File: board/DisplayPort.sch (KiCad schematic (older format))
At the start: 15 parts, among them J8 DISPLAY_PORT, J9 DISPLAY_PORT

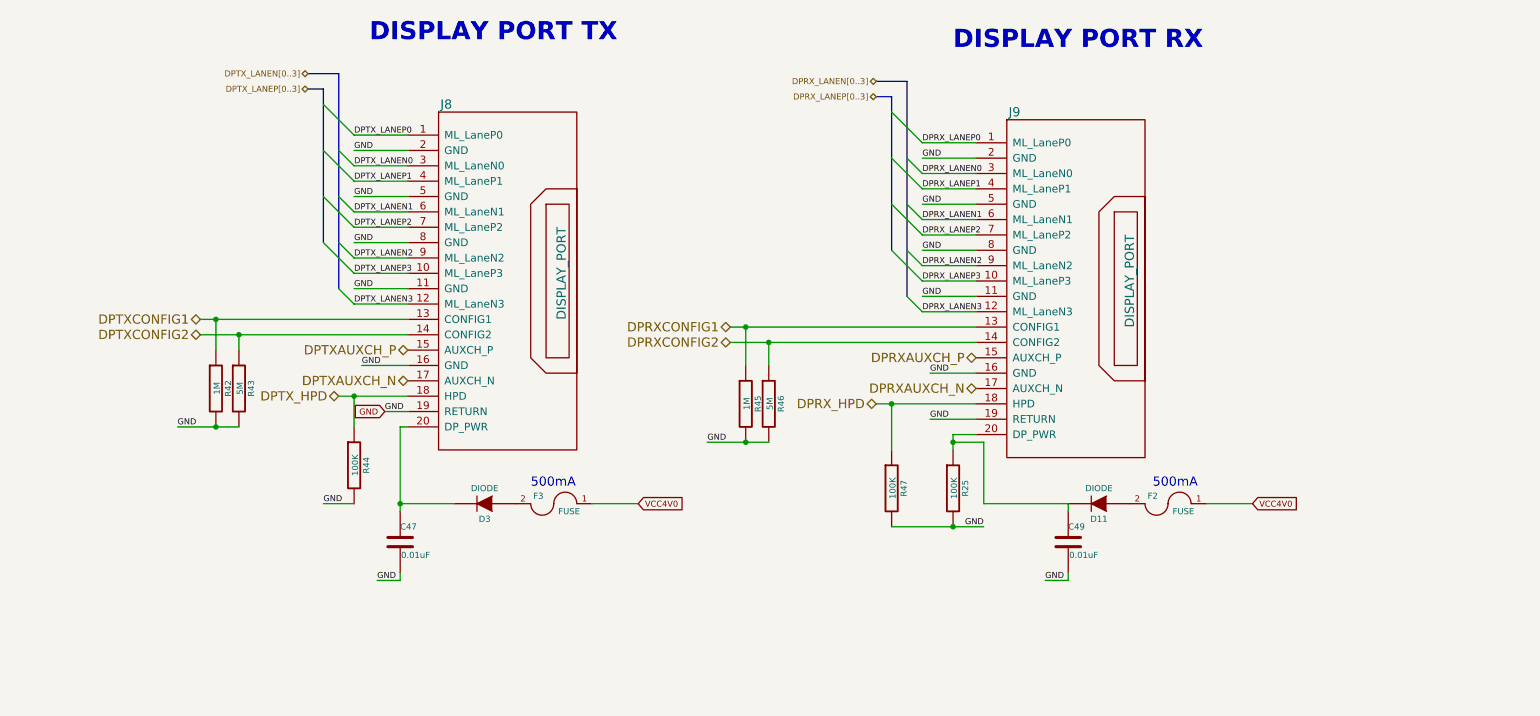
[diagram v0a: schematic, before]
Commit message: Issue #1950 - Adding DisplayPort DC blocking capacitors to schematic.
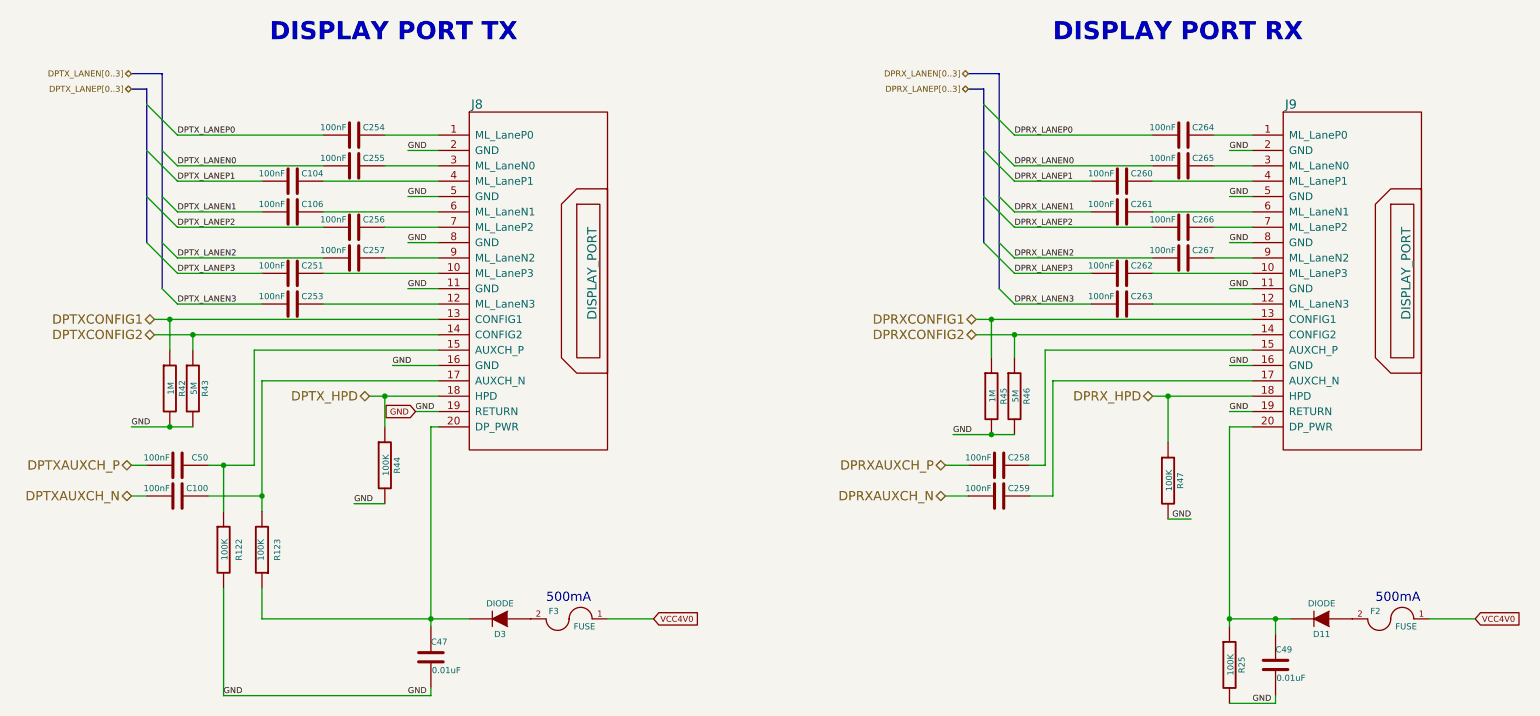
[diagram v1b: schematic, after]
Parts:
- added C100, C104, C106, C251, C253, C254, C255, C256, C257, C258, C259, C260, C261, C262, C263, C264, C265, C266, C267, C50: 100nF, 0402, symbol C
- added R122, R123: 100K, ~, symbol R
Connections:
- net DPRXAUXCH_N: now also C259.1; no longer J9.17 (AUXCH_N)
- net DPRXAUXCH_P: now also C258.1; no longer J9.15 (AUXCH_P)
- net DPRX_LANEN0: now also C265.1; no longer J9.3 (ML_LaneN0)
- net DPRX_LANEN1: now also C261.1; no longer J9.6 (ML_LaneN1)
- net DPRX_LANEN2: now also C267.1; no longer J9.9 (ML_LaneN2)
- net DPRX_LANEN3: now also C263.1; no longer J9.12 (ML_LaneN3)
- net DPRX_LANEP0: now also C264.1; no longer J9.1 (ML_LaneP0)
- net DPRX_LANEP1: now also C260.1; no longer J9.4 (ML_LaneP1)
- net DPRX_LANEP2: now also C266.1; no longer J9.7 (ML_LaneP2)
- net DPRX_LANEP3: now also C262.1; no longer J9.10 (ML_LaneP3)
- net DPTXAUXCH_N: now also C100.1; no longer J8.17 (AUXCH_N)
- net DPTXAUXCH_P: now also C50.1; no longer J8.15 (AUXCH_P)
- net DPTX_LANEN0: now also C255.1; no longer J8.3 (ML_LaneN0)
- net DPTX_LANEN1: now also C106.1; no longer J8.6 (ML_LaneN1)
- net DPTX_LANEN2: now also C257.1; no longer J8.9 (ML_LaneN2)
- net DPTX_LANEN3: now also C253.1; no longer J8.12 (ML_LaneN3)
- net DPTX_LANEP0: now also C254.1; no longer J8.1 (ML_LaneP0)
- net DPTX_LANEP1: now also C104.1; no longer J8.4 (ML_LaneP1)
- net DPTX_LANEP2: now also C256.1; no longer J8.7 (ML_LaneP2)
- net DPTX_LANEP3: now also C251.1; no longer J8.10 (ML_LaneP3)
- net GND: now also R122.2
- net at C47.1, D3.2 (K), J8.20 (DP_PWR): now also R123.1
- new net: C254.2, J8.1 (ML_LaneP0)
- new net: C251.2, J8.10 (ML_LaneP3)
- new net: C253.2, J8.12 (ML_LaneN3)
- new net: C50.2, J8.15 (AUXCH_P), R122.1
- new net: C100.2, J8.17 (AUXCH_N), R123.2
- new net: C255.2, J8.3 (ML_LaneN0)
- new net: C104.2, J8.4 (ML_LaneP1)
- new net: C106.2, J8.6 (ML_LaneN1)
- new net: C256.2, J8.7 (ML_LaneP2)
- new net: C257.2, J8.9 (ML_LaneN2)
- new net: C264.2, J9.1 (ML_LaneP0)
- new net: C262.2, J9.10 (ML_LaneP3)
- new net: C263.2, J9.12 (ML_LaneN3)
- new net: C258.2, J9.15 (AUXCH_P)
- new net: C259.2, J9.17 (AUXCH_N)
- new net: C265.2, J9.3 (ML_LaneN0)
- new net: C260.2, J9.4 (ML_LaneP1)
- new net: C261.2, J9.6 (ML_LaneN1)
- new net: C266.2, J9.7 (ML_LaneP2)
- new net: C267.2, J9.9 (ML_LaneN2)
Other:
- moved on the sheet: C47, C49, D11, D3, F2, F3, J8, J9, R25, R42, R43, R44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

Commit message: Importing footprint names into schematic.
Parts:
- C47, C49, F2, F3, R25, R42, R43, R44, R45, R46, R47: footprint ~ -> SM0603
- D11, D3: footprint ~ -> DO-214AC(SMA)
- J8, J9: footprint ~ -> Display_Port
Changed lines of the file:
@@
 Sheet 6 12
 Title "HDMI2USB"
-Date "5 jul 2015"
+Date "23 jul 2015"
 Rev "Rev2"
 Comp ""
@@
 F 0 "J8" H 3800 4050 60  0000 C CNN
 F 1 "DISPLAY_PORT" V 4550 2950 60  0000 C CNN
-F 2 "~" H 4350 2950 60  0000 C CNN
+F 2 "Display_Port" H 4350 2950 60  0001 C CNN
 F 3 "~" H 4350 2950 60  0000 C CNN
 F 4 "Yes" H 4400 2950 60  0001 C CNN "Populate"
@@
 F 0 "J9" H 9100 4050 60  0000 C CNN
 F 1 "DISPLAY_PORT" V 9850 2950 60  0000 C CNN
-F 2 "~" H 9650 2950 60  0000 C CNN
+F 2 "Display_Port" H 9650 2950 60  0001 C CNN
 F 3 "~" H 9650 2950 60  0000 C CNN
 F 4 "Yes" H 9650 2950 60  0001 C CNN "Populate"
@@
 F 0 "R25" V 8780 5500 40  0000 C CNN
 F 1 "100K" V 8707 5501 40  0000 C CNN
-F 2 "~" V 8630 5500 30  0000 C CNN
+F 2 "SM0603" V 8630 5500 30  0001 C CNN
 F 3 "~" H 8700 5500 30  0000 C CNN
 F 4 "Yes" H 8700 5500 30  0001 C CNN "Populate"
@@
 F 0 "F3" H 4500 5250 40  0000 C CNN
 F 1 "FUSE" H 4300 5150 40  0000 C CNN
-F 2 "~" H 4400 5200 60  0000 C CNN
+F 2 "SM0603" H 4400 5200 60  0001 C CNN
 F 3 "~" H 4400 5200 60  0000 C CNN
 F 4 "Yes" H 4400 5200 60  0001 C CNN "Populate"
@@
 F 0 "R42" V 1880 3700 40  0000 C CNN
 F 1 "1M" V 1807 3701 40  0000 C CNN
-F 2 "~" V 1730 3700 30  0000 C CNN
+F 2 "SM0603" V 1730 3700 30  0001 C CNN
 F 3 "~" H 1800 3700 30  0000 C CNN
 F 4 "Yes" H 1800 3700 30  0001 C CNN "Populate"
@@
 F 0 "R43" V 2030 3700 40  0000 C CNN
 F 1 "5M" V 1957 3701 40  0000 C CNN
-F 2 "~" V 1880 3700 30  0000 C CNN
+F 2 "SM0603" V 1880 3700 30  0001 C CNN
 F 3 "~" H 1950 3700 30  0000 C CNN
 F 4 "Yes" H 1950 3700 30  0001 C CNN "Populate"
@@
 F 0 "R45" V 7230 3750 40  0000 C CNN
 F 1 "1M" V 7157 3751 40  0000 C CNN
-F 2 "~" V 7080 3750 30  0000 C CNN
+F 2 "SM0603" V 7080 3750 30  0001 C CNN
 F 3 "~" H 7150 3750 30  0000 C CNN
 F 4 "Yes" H 7150 3750 30  0001 C CNN "Populate"
@@
 F 0 "R46" V 7380 3750 40  0000 C CNN
 F 1 "5M" V 7307 3751 40  0000 C CNN
-F 2 "~" V 7230 3750 30  0000 C CNN
+F 2 "SM0603" V 7230 3750 30  0001 C CNN
 F 3 "~" H 7300 3750 30  0000 C CNN
 F 4 "Yes" H 7300 3750 30  0001 C CNN "Populate"
@@
 F 0 "R47" V 8380 4300 40  0000 C CNN
 F 1 "100K" V 8307 4301 40  0000 C CNN
-F 2 "~" V 8230 4300 30  0000 C CNN
+F 2 "SM0603" V 8230 4300 30  0001 C CNN
 F 3 "~" H 8300 4300 30  0000 C CNN
 F 4 "Yes" H 8300 4300 30  0001 C CNN "Populate"
@@
 F 0 "R44" V 3280 4200 40  0000 C CNN
 F 1 "100K" V 3207 4201 40  0000 C CNN
-F 2 "~" V 3130 4200 30  0000 C CNN
+F 2 "SM0603" V 3130 4200 30  0001 C CNN
 F 3 "~" H 3200 4200 30  0000 C CNN
 F 4 "Yes" H 3200 4200 30  0001 C CNN "Populate"
@@
 F 0 "D3" H 3950 5300 40  0000 C CNN
 F 1 "DIODE" H 3950 5100 40  0000 C CNN
-F 2 "~" H 3950 5200 60  0000 C CNN
+F 2 "DO-214AC(SMA)" H 3950 5200 60  0001 C CNN
 F 3 "~" H 3950 5200 60  0000 C CNN
 F 4 "Yes" H 3950 5200 60  0001 C CNN "Populate"
@@
 F 0 "F2" H 9850 5250 40  0000 C CNN
 F 1 "FUSE" H 9650 5150 40  0000 C CNN
-F 2 "~" H 9750 5200 60  0000 C CNN
+F 2 "SM0603" H 9750 5200 60  0001 C CNN
 F 3 "~" H 9750 5200 60  0000 C CNN
 F 4 "Yes" H 9750 5200 60  0001 C CNN "Populate"
@@
 F 0 "D11" H 9300 5300 40  0000 C CNN
 F 1 "DIODE" H 9300 5100 40  0000 C CNN
-F 2 "~" H 9300 5200 60  0000 C CNN
+F 2 "DO-214AC(SMA)" H 9300 5200 60  0001 C CNN
 F 3 "~" H 9300 5200 60  0000 C CNN
 F 4 "Yes" H 9300 5200 60  0001 C CNN "Populate"
@@
 F 0 "C47" H 3500 5550 40  0000 L CNN
 F 1 "0.01uF" H 3506 5365 40  0000 L CNN
-F 2 "~" H 3538 5300 30  0000 C CNN
+F 2 "SM0603" H 3538 5300 30  0001 C CNN
 F 3 "~" H 3500 5450 60  0000 C CNN
 F 4 "Yes" H 3500 5450 60  0001 C CNN "Populate"
@@
 F 0 "C49" H 9000 5600 40  0000 L CNN
 F 1 "0.01uF" H 9006 5415 40  0000 L CNN
-F 2 "~" H 9038 5350 30  0000 C CNN
+F 2 "SM0603" H 9038 5350 30  0001 C CNN
 F 3 "~" H 9000 5500 60  0000 C CNN
 F 4 "Yes" H 9000 5500 60  0001 C CNN "Populate"

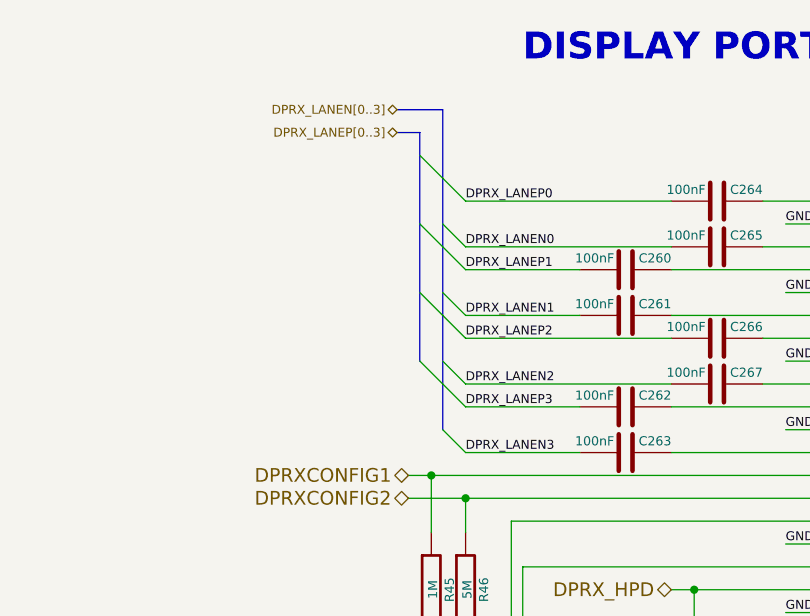
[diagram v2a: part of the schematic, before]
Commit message: Issue #9
Added DC blocking capacitors, VTTREF issue solved, 5V power common
connection issue solved
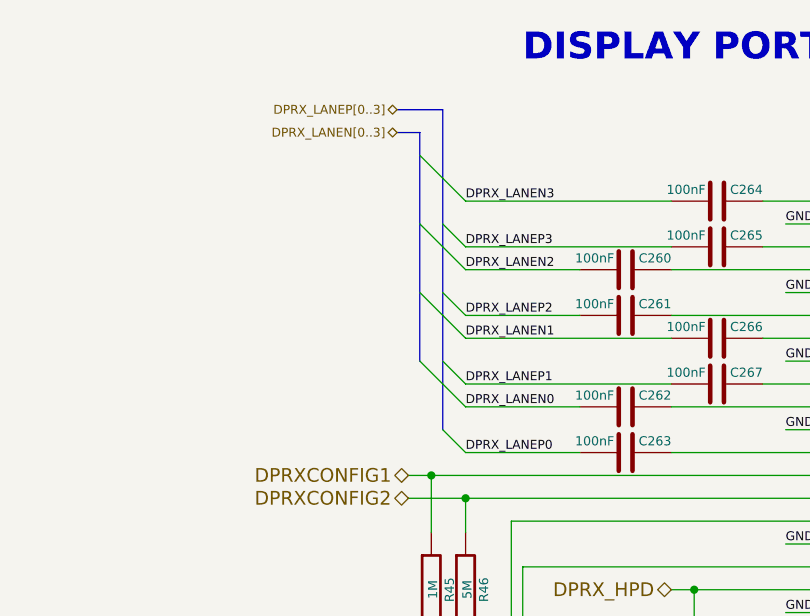
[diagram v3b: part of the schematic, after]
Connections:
- net DPRX_LANEN0: now also C262.1; no longer C265.1
- net DPRX_LANEN1: now also C266.1; no longer C261.1
- net DPRX_LANEN2: now also C260.1; no longer C267.1
- net DPRX_LANEN3: now also C264.1; no longer C263.1
- net DPRX_LANEP0: now also C263.1; no longer C264.1
- net DPRX_LANEP1: now also C267.1; no longer C260.1
- net DPRX_LANEP2: now also C261.1; no longer C266.1
- net DPRX_LANEP3: now also C265.1; no longer C262.1
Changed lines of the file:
@@
 Sheet 6 12
 Title "HDMI2USB"
-Date "23 jul 2015"
+Date "10 sep 2015"
 Rev "Rev2"
 Comp ""
@@
 	1    0    0    -1
 $EndComp
-Text Label 7300 2050 0    39   ~ 0
+Text Label 7300 3150 0    39   ~ 0
 DPRX_LANEP0
-Text Label 7300 2350 0    39   ~ 0
+Text Label 7300 2850 0    39   ~ 0
 DPRX_LANEP1
-Text Label 7300 2650 0    39   ~ 0
+Text Label 7300 2550 0    39   ~ 0
 DPRX_LANEP2
-Text Label 7300 2950 0    39   ~ 0
+Text Label 7300 2250 0    39   ~ 0
 DPRX_LANEP3
 Text Label 1850 2050 0    39   ~ 0
@@
 Text Label 1850 2950 0    39   ~ 0
 DPTX_LANEP3
-Text Label 7300 2250 0    39   ~ 0
+Text Label 7300 2950 0    39   ~ 0
 DPRX_LANEN0
-Text Label 7300 2550 0    39   ~ 0
+Text Label 7300 2650 0    39   ~ 0
 DPRX_LANEN1
-Text Label 7300 2850 0    39   ~ 0
+Text Label 7300 2350 0    39   ~ 0
 DPRX_LANEN2
-Text Label 7300 3150 0    39   ~ 0
+Text Label 7300 2050 0    39   ~ 0
 DPRX_LANEN3
 Text Label 1850 2250 0    39   ~ 0
@@
 Text GLabel 3400 3850 0    39   Input ~ 0
 GND
+Text HLabel 7000 1650 0    39   BiDi ~ 0
+DPRX_LANEP[0..3]
 Text HLabel 7000 1750 0    39   BiDi ~ 0
-DPRX_LANEP[0..3]
-Text HLabel 7000 1650 0    39   BiDi ~ 0
 DPRX_LANEN[0..3]
 Text HLabel 1550 1750 0    39   BiDi ~ 0

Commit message: Final changes
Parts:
- C100, C104, C106, C251, C253, C254, C255, C256, C257, C258, C259, C260, C261, C262, C263, C264, C265, C266, C267, C50: value 100nF -> 0.1uF
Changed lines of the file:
@@
 LIBS:contrib
 LIBS:valves
-LIBS:hdmi2usb
-LIBS:timvideos-pcie-8x
 LIBS:HDMI2USB-cache
 EELAYER 27 0
@@
 Sheet 6 12
 Title "HDMI2USB"
-Date "2 nov 2015"
+Date "9 nov 2015"
 Rev "Rev2"
 Comp ""
@@
 P 8400 2050
 F 0 "C264" V 8350 1850 40  0000 L CNN
-F 1 "100nF" V 8350 2100 40  0000 L CNN
+F 1 "0.1uF" V 8350 2100 40  0000 L CNN
 F 2 "0402" H 8438 1900 30  0001 C CNN
 F 3 "~" H 8400 2050 60  0000 C CNN
@@
 P 8400 2250
 F 0 "C265" V 8350 2050 40  0000 L CNN
-F 1 "100nF" V 8350 2300 40  0000 L CNN
+F 1 "0.1uF" V 8350 2300 40  0000 L CNN
 F 2 "0402" H 8438 2100 30  0001 C CNN
 F 3 "~" H 8400 2250 60  0000 C CNN
@@
 P 8000 2350
 F 0 "C260" V 7950 2150 40  0000 L CNN
-F 1 "100nF" V 7950 2400 40  0000 L CNN
+F 1 "0.1uF" V 7950 2400 40  0000 L CNN
 F 2 "0402" H 8038 2200 30  0001 C CNN
 F 3 "~" H 8000 2350 60  0000 C CNN
@@
 P 8000 2550
 F 0 "C261" V 7950 2350 40  0000 L CNN
-F 1 "100nF" V 7950 2600 40  0000 L CNN
+F 1 "0.1uF" V 7950 2600 40  0000 L CNN
 F 2 "0402" H 8038 2400 30  0001 C CNN
 F 3 "~" H 8000 2550 60  0000 C CNN
@@
 P 8400 2650
 F 0 "C266" V 8350 2450 40  0000 L CNN
-F 1 "100nF" V 8350 2700 40  0000 L CNN
+F 1 "0.1uF" V 8350 2700 40  0000 L CNN
 F 2 "0402" H 8438 2500 30  0001 C CNN
 F 3 "~" H 8400 2650 60  0000 C CNN
@@
 P 8400 2850
 F 0 "C267" V 8350 2650 40  0000 L CNN
-F 1 "100nF" V 8350 2900 40  0000 L CNN
+F 1 "0.1uF" V 8350 2900 40  0000 L CNN
 F 2 "0402" H 8438 2700 30  0001 C CNN
 F 3 "~" H 8400 2850 60  0000 C CNN
@@
 P 8000 2950
 F 0 "C262" V 7950 2750 40  0000 L CNN
-F 1 "100nF" V 7950 3000 40  0000 L CNN
+F 1 "0.1uF" V 7950 3000 40  0000 L CNN
 F 2 "0402" H 8038 2800 30  0001 C CNN
 F 3 "~" H 8000 2950 60  0000 C CNN
@@
 P 8000 3150
 F 0 "C263" V 7950 2950 40  0000 L CNN
-F 1 "100nF" V 7950 3200 40  0000 L CNN
+F 1 "0.1uF" V 7950 3200 40  0000 L CNN
 F 2 "0402" H 8038 3000 30  0001 C CNN
 F 3 "~" H 8000 3150 60  0000 C CNN
@@
 P 3000 2050
 F 0 "C254" V 2950 1850 40  0000 L CNN
-F 1 "100nF" V 2950 2100 40  0000 L CNN
+F 1 "0.1uF" V 2950 2100 40  0000 L CNN
 F 2 "0402" H 3038 1900 30  0001 C CNN
 F 3 "~" H 3000 2050 60  0000 C CNN
@@
 P 3000 2250
 F 0 "C255" V 2950 2050 40  0000 L CNN
-F 1 "100nF" V 2950 2300 40  0000 L CNN
+F 1 "0.1uF" V 2950 2300 40  0000 L CNN
 F 2 "0402" H 3038 2100 30  0001 C CNN
 F 3 "~" H 3000 2250 60  0000 C CNN
@@
 P 2600 2350
 F 0 "C104" V 2550 2150 40  0000 L CNN
-F 1 "100nF" V 2550 2400 40  0000 L CNN
+F 1 "0.1uF" V 2550 2400 40  0000 L CNN
 F 2 "0402" H 2638 2200 30  0001 C CNN
 F 3 "~" H 2600 2350 60  0000 C CNN
@@
 P 2600 2550
 F 0 "C106" V 2550 2350 40  0000 L CNN
-F 1 "100nF" V 2550 2600 40  0000 L CNN
+F 1 "0.1uF" V 2550 2600 40  0000 L CNN
 F 2 "0402" H 2638 2400 30  0001 C CNN
 F 3 "~" H 2600 2550 60  0000 C CNN
@@
 P 3000 2650
 F 0 "C256" V 2950 2450 40  0000 L CNN
-F 1 "100nF" V 2950 2700 40  0000 L CNN
+F 1 "0.1uF" V 2950 2700 40  0000 L CNN
 F 2 "0402" H 3038 2500 30  0001 C CNN
 F 3 "~" H 3000 2650 60  0000 C CNN
@@
 P 3000 2850
 F 0 "C257" V 2950 2650 40  0000 L CNN
-F 1 "100nF" V 2950 2900 40  0000 L CNN
+F 1 "0.1uF" V 2950 2900 40  0000 L CNN
 F 2 "0402" H 3038 2700 30  0001 C CNN
 F 3 "~" H 3000 2850 60  0000 C CNN
@@
 P 2600 2950
 F 0 "C251" V 2550 2750 40  0000 L CNN
-F 1 "100nF" V 2550 3000 40  0000 L CNN
+F 1 "0.1uF" V 2550 3000 40  0000 L CNN
 F 2 "0402" H 2638 2800 30  0001 C CNN
 F 3 "~" H 2600 2950 60  0000 C CNN
@@
 P 2600 3150
 F 0 "C253" V 2550 2950 40  0000 L CNN
-F 1 "100nF" V 2550 3200 40  0000 L CNN
+F 1 "0.1uF" V 2550 3200 40  0000 L CNN
 F 2 "0402" H 2638 3000 30  0001 C CNN
 F 3 "~" H 2600 3150 60  0000 C CNN
@@
 P 1850 4200
 F 0 "C50" V 1800 4000 40  0000 L CNN
-F 1 "100nF" V 1800 4250 40  0000 L CNN
+F 1 "0.1uF" V 1800 4250 40  0000 L CNN
 F 2 "0402" H 1888 4050 30  0001 C CNN
 F 3 "~" H 1850 4200 60  0000 C CNN
@@
 P 1850 4400
 F 0 "C100" V 1800 4200 40  0000 L CNN
-F 1 "100nF" V 1800 4450 40  0000 L CNN
+F 1 "0.1uF" V 1800 4450 40  0000 L CNN
 F 2 "0402" H 1888 4250 30  0001 C CNN
 F 3 "~" H 1850 4400 60  0000 C CNN
@@
 P 7200 4200
 F 0 "C258" V 7150 4000 40  0000 L CNN
-F 1 "100nF" V 7150 4250 40  0000 L CNN
+F 1 "0.1uF" V 7150 4250 40  0000 L CNN
 F 2 "0402" H 7238 4050 30  0001 C CNN
 F 3 "~" H 7200 4200 60  0000 C CNN
@@
 P 7200 4400
 F 0 "C259" V 7150 4200 40  0000 L CNN
-F 1 "100nF" V 7150 4450 40  0000 L CNN
+F 1 "0.1uF" V 7150 4450 40  0000 L CNN
 F 2 "0402" H 7238 4250 30  0001 C CNN
 F 3 "~" H 7200 4400 60  0000 C CNN
